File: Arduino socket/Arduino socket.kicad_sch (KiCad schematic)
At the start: 2 parts, among them J3 Conn_01x06_Socket

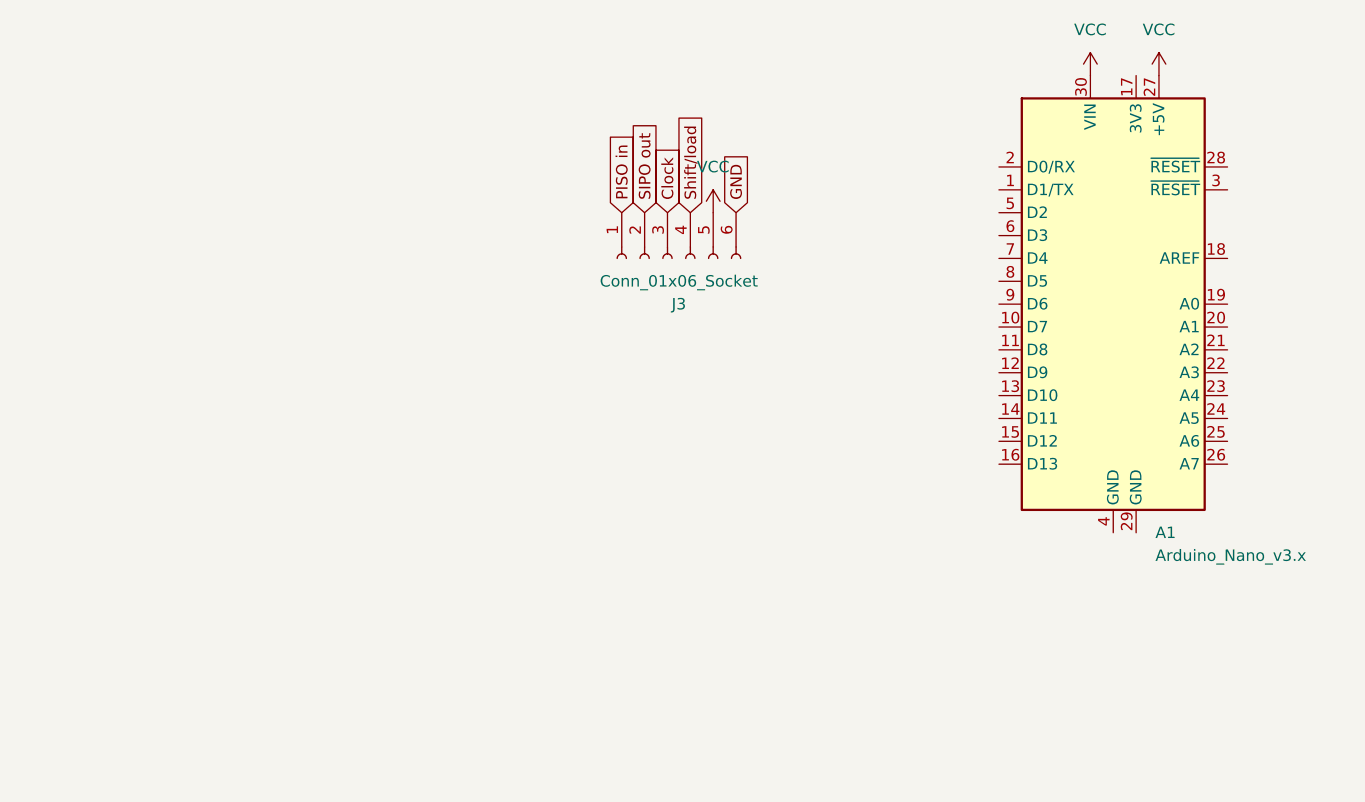
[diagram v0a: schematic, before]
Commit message: Started coding.
Reading and writing to registers implemented.
The circuit is now on rev 1.1, but there were some mistakes on this one to, hehe.
The dip-switch is NOT the same size as a 16p soic, a little wider (bodgedd by bending pins under on one side (the one thats just all vcc anyways, as it can be bridged if you're struggeling with the jank solder)).
The socket also has some mechanical solder points on the ends, that wasnt on my footprint. They are also thinner and longer than thought. The mechanical solder on one side could short some pins on the 165, but i simply put a piece of kapton tape acrross the pins. Circuit works otherwise. Perhaps a little hot. Maybe not ideal to drive LEDs directly from 595's, but they can probably handle it
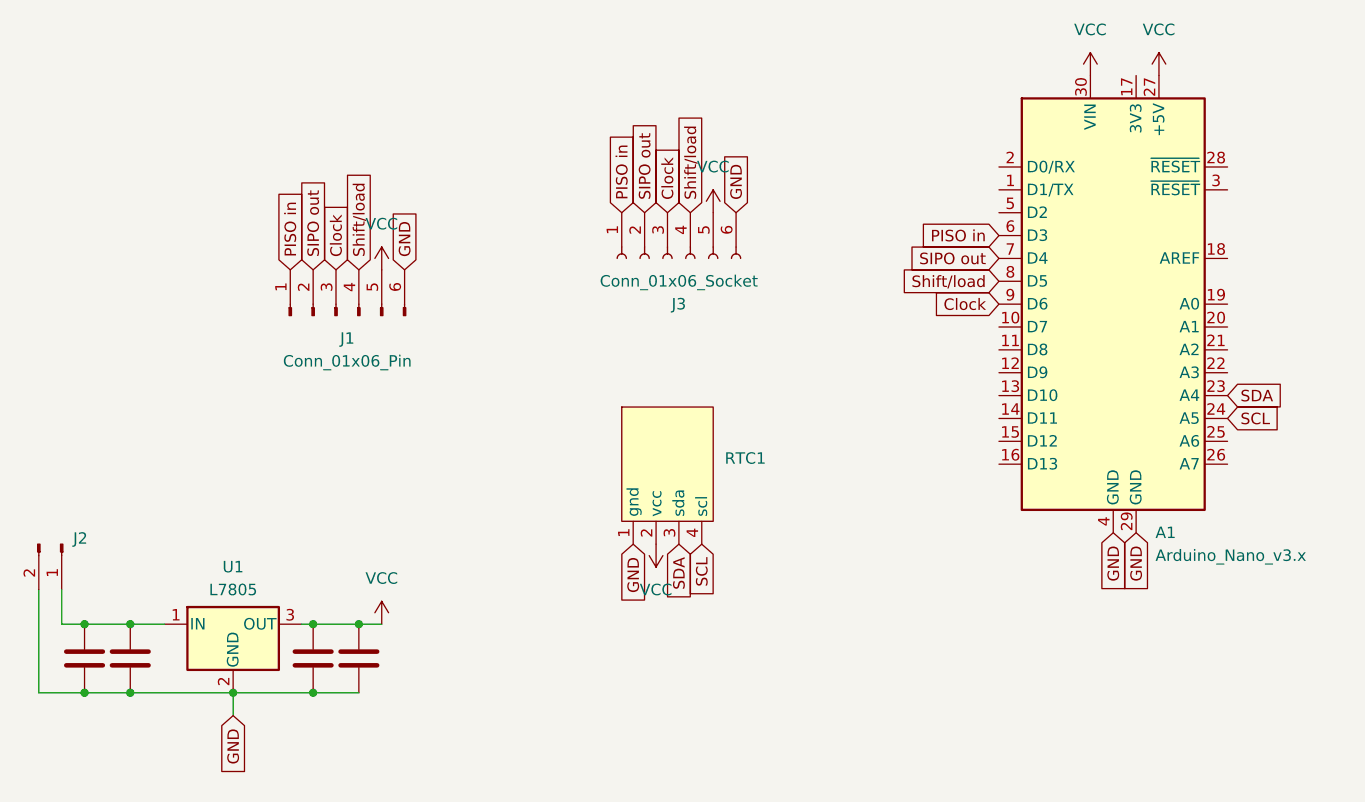
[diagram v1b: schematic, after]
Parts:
- added C1, C2, C3, C4: C, Capacitor_SMD:C_0805_2012Metric_Pad1.18x1.45mm_HandSolder, symbol Device:C
- added J1: Conn_01x06_Pin, Connector_PinHeader_2.54mm:PinHeader_1x06_P2.54mm_Horizontal, symbol Connector:Conn_01x06_Pin
- added J2: Conn_01x02_Pin, Connector_PinHeader_2.54mm:PinHeader_1x02_P2.54mm_Vertical, symbol Connector:Conn_01x02_Pin
- added RTC1: ~, timezoneClock:DS3231 RTC module, symbol timeZoneClock:DS3231_RTC_module
- added U1: L7805, Package_TO_SOT_THT:TO-220-3_Horizontal_TabDown, symbol Regulator_Linear:L7805
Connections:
- net Clock: now also A1.9 (D6), J1.3 (Pin_3)
- net GND: now also A1.29 (GND), A1.4 (GND), C1.2, C2.2, C3.2, C4.2, J1.6 (Pin_6), J2.2 (Pin_2), RTC1.1 (gnd), U1.2 (GND)
- net PISO in: now also A1.6 (D3), J1.1 (Pin_1)
- net SIPO out: now also A1.7 (D4), J1.2 (Pin_2)
- net Shift/load: now also A1.8 (D5), J1.4 (Pin_4)
- net VCC: now also C3.1, C4.1, J1.5 (Pin_5), RTC1.2 (vcc), U1.3 (OUT)
- net SDA: now reaches A1.23 (A4)
- net SDA: now also RTC1.3 (sda)
- net SCL: now reaches A1.24 (A5)
- net SCL: now also RTC1.4 (scl)
- new net: C1.1, C2.1, J2.1 (Pin_1), U1.1 (IN)
